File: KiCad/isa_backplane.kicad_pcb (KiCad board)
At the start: 2 copper layers, 116.8 x 154.9 mm, 61 parts, among them P1 POWER, P2 POWER_SW, P3 POWER_LED, SW1 POWER, U1 74HCT74, U2 74HCT14, U3 LM7905CT

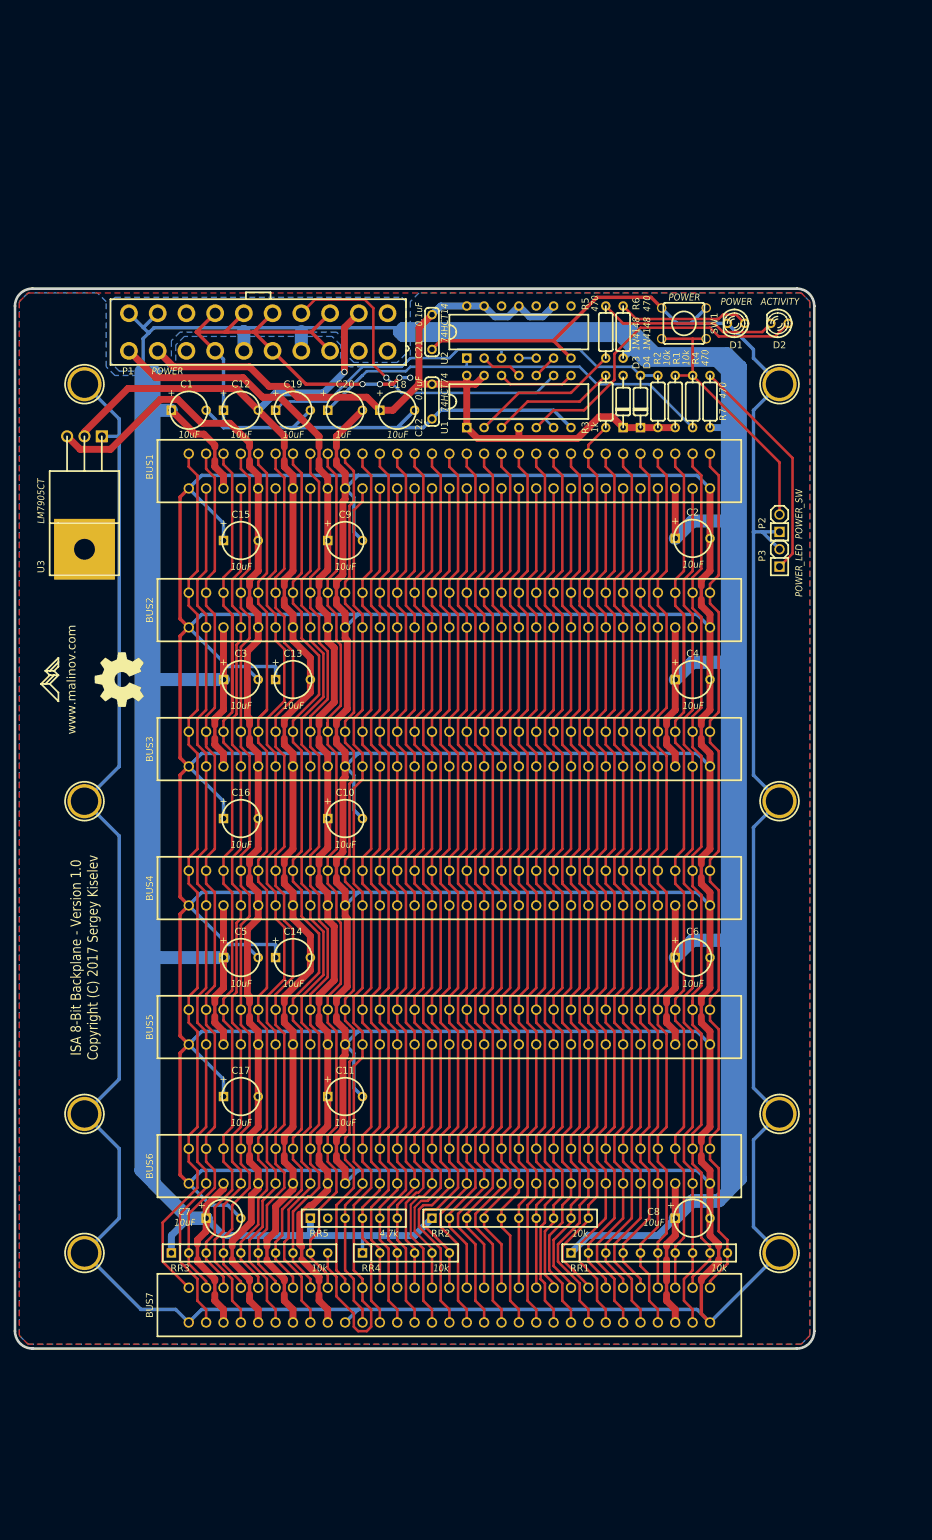
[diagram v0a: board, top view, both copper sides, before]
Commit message: Add two ISA slots
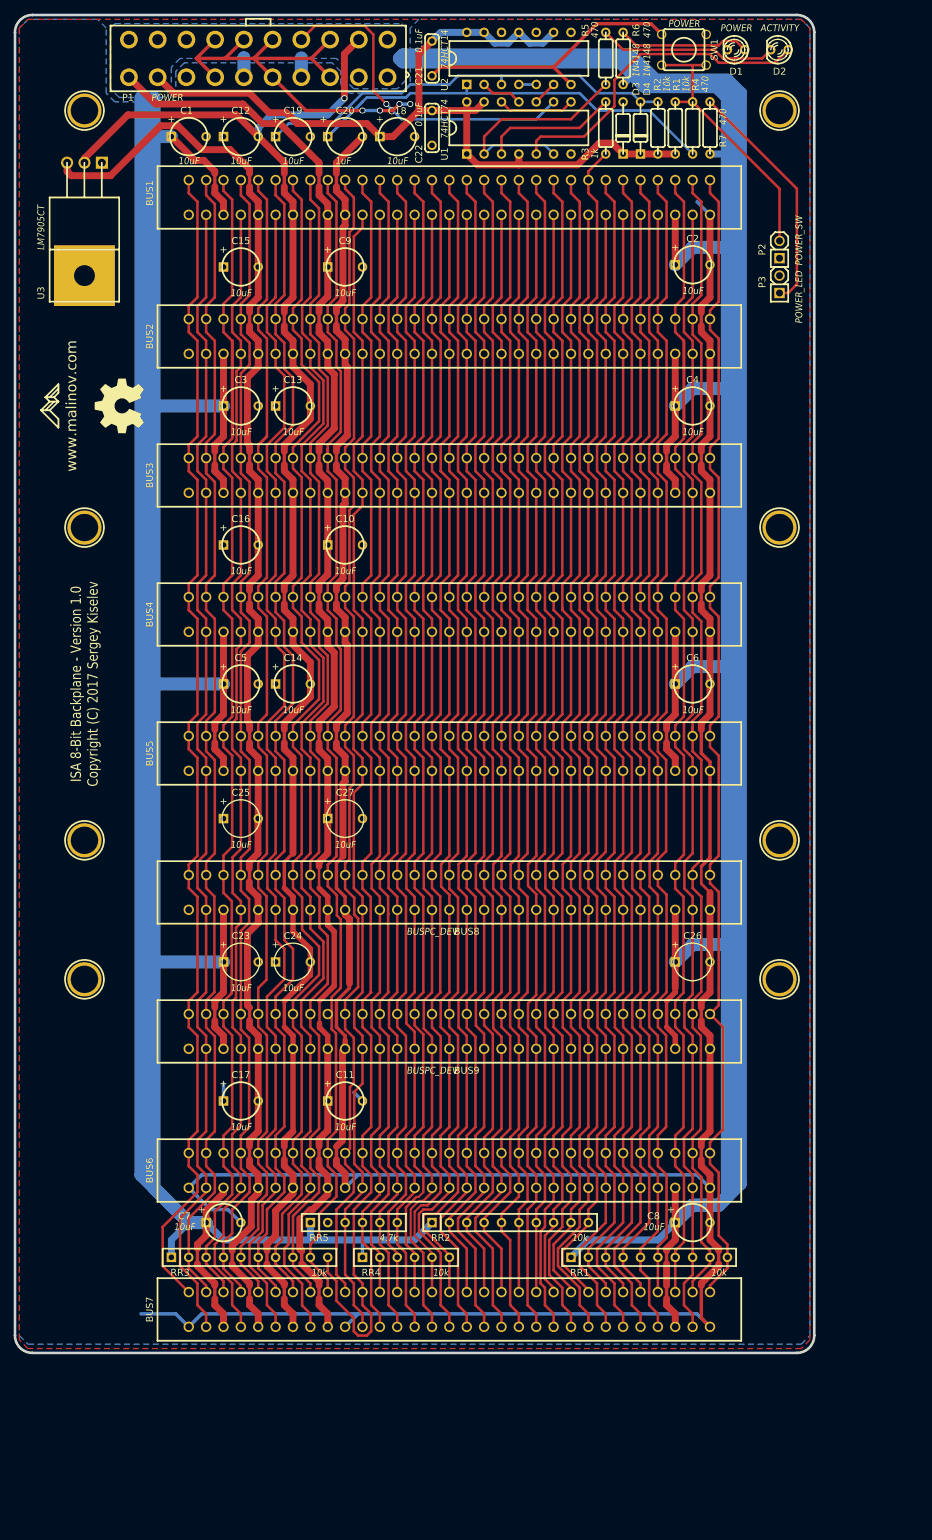
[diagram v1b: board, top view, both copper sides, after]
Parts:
- added BUS8: BUSPC_DEV, My_Components:Conn_Edge_ISA8, F.Cu at (114.3, 139.1)
- added BUS9: BUSPC_DEV, My_Components:Conn_Edge_ISA8, F.Cu at (114.3, 159.4)
- added C23: 10uF, My_Components:Cap_Tant_508, F.Cu at (83.8, 149.2)
- added C24: 10uF, My_Components:Cap_Tant_508, F.Cu at (91.4, 149.2)
- added C25: 10uF, My_Components:Cap_Tant_508, F.Cu at (83.8, 128.3)
- added C26: 10uF, My_Components:Cap_Tant_508, F.Cu at (149.9, 149.2)
- added C27: 10uF, My_Components:Cap_Tant_508, F.Cu at (99.1, 128.3)
- moved C10 40.0 mm to (99.1, 88.3)
- moved C16 40.0 mm to (83.8, 88.3)
- moved BUS2 40.0 mm to (114.3, 57.8)
- moved BUS1 40.0 mm to (114.3, 37.5)
- moved BUS3 40.0 mm to (114.3, 78.1)
- moved BUS4 40.0 mm to (114.3, 98.4)
- moved BUS5 40.0 mm to (114.3, 118.8)
- moved C1 40.0 mm to (76.2, 28.6)
- moved C12 40.0 mm to (83.8, 28.6)
- moved C13 40.0 mm to (91.4, 68.0)
- moved C14 40.0 mm to (91.4, 108.6)
- moved C18 40.0 mm to (106.7, 28.6)
- moved C19 40.0 mm to (91.4, 28.6)
- moved C2 40.0 mm to (149.9, 47.3)
- moved C20 40.0 mm to (99.1, 28.6)
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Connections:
- net /~0WS renamed /~{0WS}
- net /~DACK0 renamed /~{DACK0}
- net /~DACK1 renamed /~{DACK1}
- net /~DACK2 renamed /~{DACK2}
- net /~DACK3 renamed /~{DACK3}
- net /~IOCHK renamed /~{IOCHK}
- net /~IOR renamed /~{IOR}
- net /~IOW renamed /~{IOW}
- net /~MEMR renamed /~{MEMR}
- net /~MEMW renamed /~{MEMW}
- net /~PS_ON renamed /~{PS_ON}
- P1 pad 1: Net-(P1-Pad1) -> unconnected-(P1-3.3V-Pad1)
- P1 pad 11: Net-(P1-Pad11) -> unconnected-(P1-3.3V-Pad11)
- P1 pad 2: Net-(P1-Pad2) -> unconnected-(P1-3.3V-Pad2)
- P1 pad 8: Net-(P1-Pad8) -> unconnected-(P1-PWR_OK-Pad8)
- RR5 pad 2: Net-(RR5-Pad2) -> unconnected-(RR5-Pad2)
- U2 pad 10: Net-(U2-Pad10) -> unconnected-(U2-Pad10)
- U2 pad 12: Net-(U2-Pad12) -> unconnected-(U2-Pad12)
- U2 pad 8: Net-(U2-Pad8) -> unconnected-(U2-Pad8)
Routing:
- net GND: track 1559.7 -> 630.6 mm
- net /+5V: track 951.6 -> 1125.0 mm
- net /-12V: track 204.3 -> 249.9 mm
- net /D2: track 134.5 -> 179.4 mm
- net /-5V: track 171.2 -> 215.5 mm
- net /~{0WS}: track 133.8 -> 177.8 mm
- net /D3: track 132.4 -> 176.2 mm
- net /D1: track 136.4 -> 180.2 mm
- net /DRQ2: track 132.4 -> 176.2 mm
- net /12V: track 173.5 -> 216.9 mm
- net /A0: track 129.3 -> 172.6 mm
- net /IORDY: track 129.3 -> 172.6 mm
- net /A19: track 129.3 -> 172.1 mm
- net /A18: track 129.3 -> 172.0 mm
- net /A16: track 130.9 -> 173.6 mm
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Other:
- board size 116.8 x 154.9 mm -> 116.8 x 195.6 mm
- net class Default removed
- net class Power removed

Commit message: Adjust mounting holes for ATX form factor
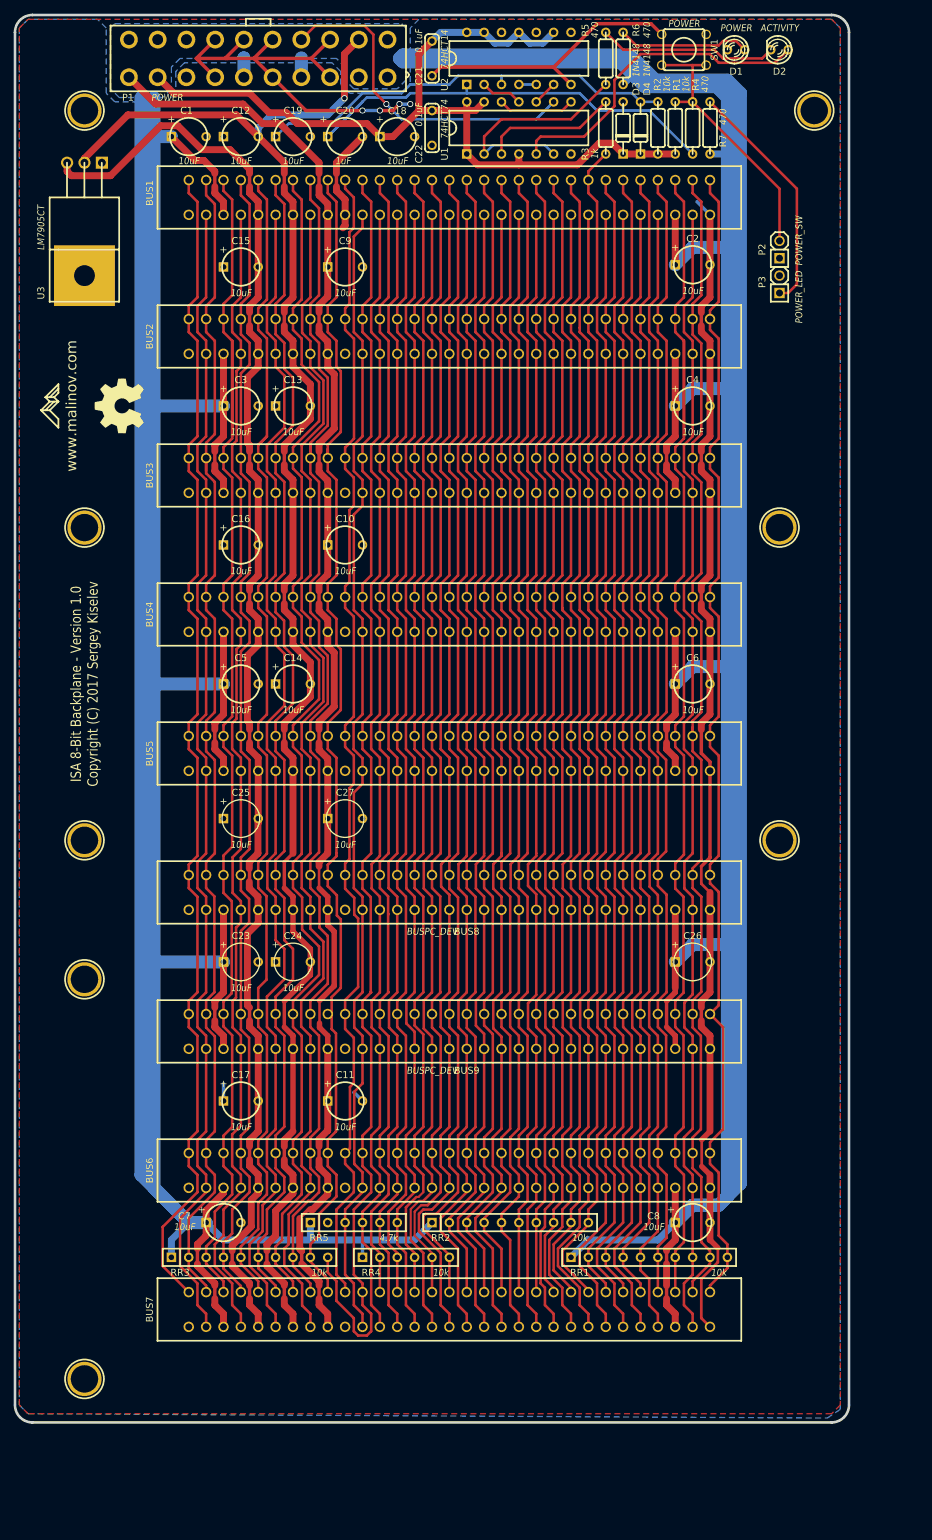
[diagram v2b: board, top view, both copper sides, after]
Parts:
- moved HOLE4 117.2 mm to (61.0, 210.2)
- moved HOLE3 5.08 mm to (167.6, 24.8)
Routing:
- net GND: track 630.6 -> 303.4 mm
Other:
- board size 116.8 x 195.6 mm -> 121.9 x 205.7 mm

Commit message: Move resistor arrays to the bottom
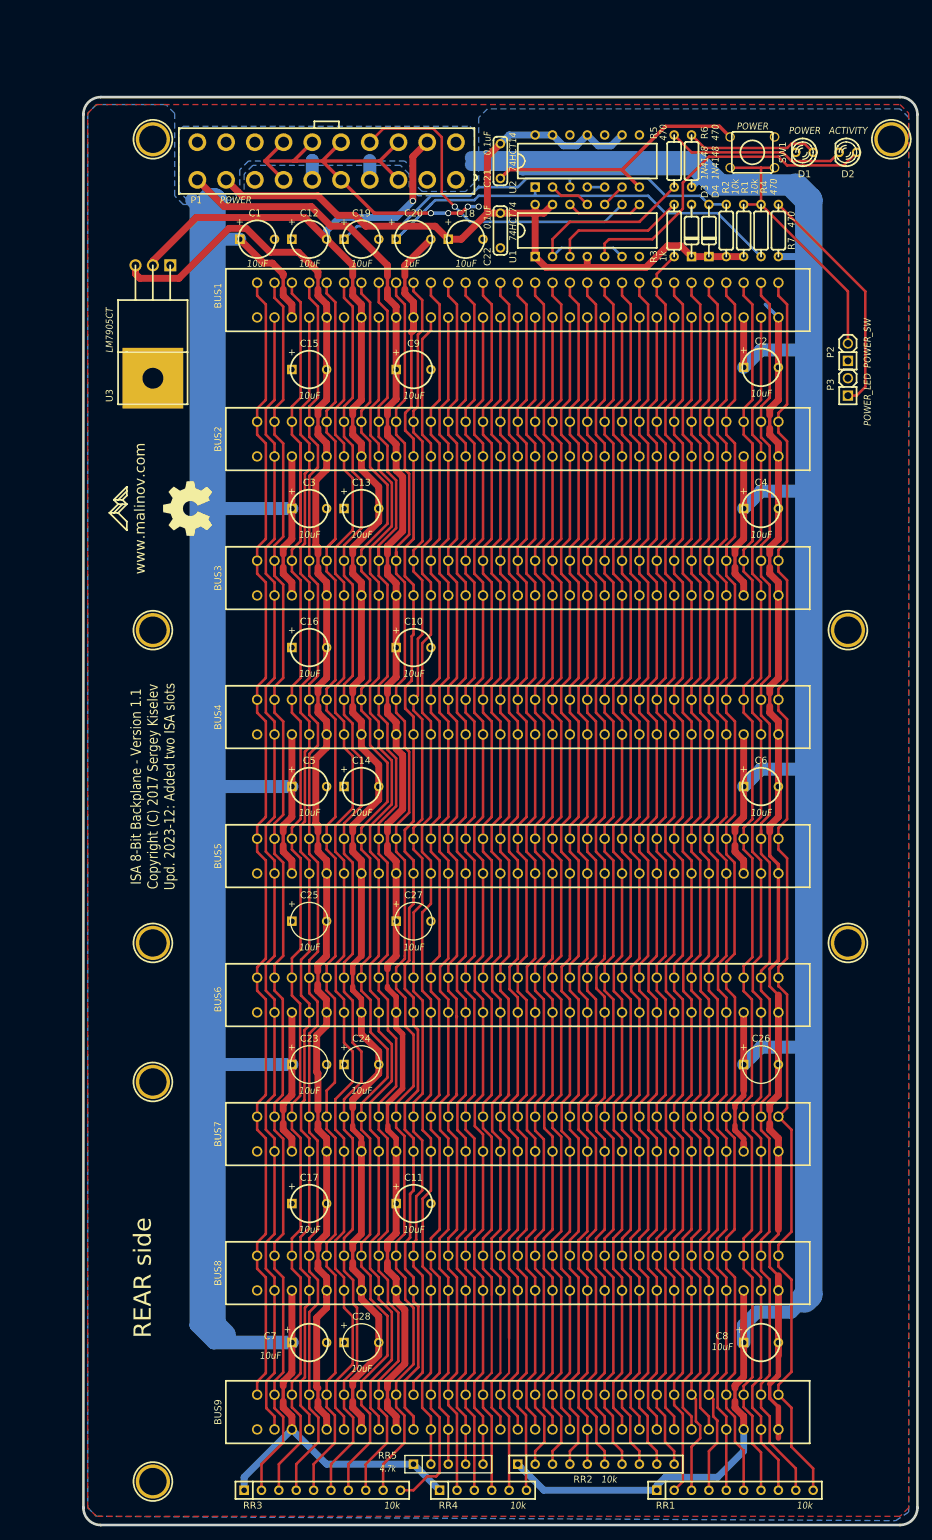
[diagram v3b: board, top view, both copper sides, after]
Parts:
- added C28: 10uF, My_Components:Cap_Tant_508, F.Cu at (101.4, 204.9)
- RR5: footprint my_components:Conn_SIL6 -> My_Components:Conn_SIL5
- moved RR5 37.9 mm to (114.1, 222.6)
- moved RR2 37.5 mm to (135.7, 222.6)
- moved RR1 36.3 mm to (156.1, 226.5)
- moved RR4 35.9 mm to (119.2, 226.5)
- moved RR3 35.7 mm to (95.7, 226.5)
- moved C7 21.6 mm to (93.8, 204.9)
- moved C8 20.2 mm to (159.9, 204.9)
- moved U1 18.0 mm to (134.5, 42.3)
- moved BUS2 18.0 mm to (124.3, 72.8)
- moved U2 18.0 mm to (134.5, 32.1)
- moved BUS1 18.0 mm to (124.3, 52.5)
- moved BUS3 18.0 mm to (124.3, 93.1)
- moved BUS4 18.0 mm to (124.3, 113.4)
- moved BUS5 18.0 mm to (124.3, 133.8)
- moved BUS6 18.0 mm to (124.3, 154.1)
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- renumbered BUS8 to BUS6, BUS9 to BUS7, BUS6 to BUS8, BUS7 to BUS9
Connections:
- RR5 pad 2: unconnected-(RR5-Pad2) -> /~{MEMW}
- RR5 pad 3: /~{MEMW} -> /~{MEMR}
- RR5 pad 4: /~{MEMR} -> /~{IOW}
- RR5 pad 5: /~{IOW} -> /~{IOR}
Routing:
- net GND: track 303.4 -> 469.3 mm
- net /+5V: track 1125.0 -> 973.3 mm
- net /D2: track 179.4 -> 195.2 mm
- net /D0: track 176.7 -> 192.4 mm
- net /A0: track 172.6 -> 188.1 mm
- net /A3: track 172.8 -> 187.8 mm
- net /A2: track 184.8 -> 199.9 mm
- net /A1: track 173.2 -> 188.3 mm
- net /D1: track 180.2 -> 195.0 mm
- net /D3: track 176.2 -> 190.5 mm
- net /D5: track 173.0 -> 186.7 mm
- net /D7: track 174.9 -> 188.6 mm
- net /D6: track 187.0 -> 200.7 mm
- net /D4: track 174.8 -> 188.5 mm
- net /A19: track 172.1 -> 185.5 mm
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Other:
- board size 121.9 x 205.7 mm -> 121.9 x 208.7 mm
- board text added: "ISA 8-Bit Backplane - Version 1.1 Copyright (C) 2017 Sergey Kiselev Upd. 2023-12: Added two ISA slots"
- board text added: "REAR side"
- board text removed: "ISA 8-Bit Backplane - Version 1.0 Copyright (C) 2017 Sergey Kiselev"

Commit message: Version 1.1
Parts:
- added HOLE10: HOLE, My_Components:Hole_4mm, F.Cu at (172.7, 225.2)
- added HOLE9: HOLE, My_Components:Hole_4mm, F.Cu at (172.7, 166.8)
- BUS1, BUS2, BUS3, BUS4, BUS5, BUS8, BUS9: footprint my_components:Conn_Edge_ISA8 -> My_Components:Conn_Edge_ISA8
- C1, C10, C11, C12, C13, C14, C15, C16, C17, C18, C19, C2, C20, C3, C4, C5, C6, C7, C8, C9: footprint my_components:Cap_Tant_508 -> My_Components:Cap_Tant_508
- C21: footprint my_components:Cap_Cer_508 -> My_Components:Cap_Cer_762
- C22: footprint my_components:Cap_Cer_508 -> My_Components:Cap_Cer_508
- D1, D2: footprint my_components:LED_3mm -> My_Components:LED_3mm
- D3, D4: footprint my_components:Diode_762 -> My_Components:Diode_762
- HOLE1, HOLE2, HOLE3, HOLE4, HOLE5, HOLE6, HOLE7, HOLE8: footprint my_components:Hole_4mm -> My_Components:Hole_4mm
- P1: footprint my_components:Conn_Power_ATX_20pin -> My_Components:Conn_Power_ATX_20pin
- P2, P3: footprint my_components:Conn_Pin_Header_2x1_2.54mm -> My_Components:Conn_Pin_Header_2x1_2.54mm
- R1, R2, R3, R4, R5, R6, R7: footprint my_components:Res_762 -> My_Components:Res_762
- RR1, RR2, RR3: footprint my_components:Conn_SIL10 -> My_Components:Conn_SIL10
- RR4: footprint my_components:Conn_SIL6 -> My_Components:Conn_SIL6
- SW1: footprint my_components:Switch_Tactile_6mm -> My_Components:Switch_Tactile_6mm
- U1, U2: footprint my_components:IC_DIP14_300 -> My_Components:IC_DIP14_300
- U3: footprint my_components:IC_TO220-3_Horiz -> My_Components:IC_TO220-3_Vert
- moved R7 12.7 mm to (172.5, 50.0), turned to 90 degrees
- moved D2 7.81 mm to (171.4, 38.6), turned to 0 degrees
- moved D1 5.26 mm to (171.4, 30.5), turned to 0 degrees
- moved C21 2.61 mm to (124.2, 31.1), turned to 90 degrees
- moved D3 2.54 mm to (152.2, 42.3)
- moved R1 2.54 mm to (159.9, 42.3)
- moved R6 2.54 mm to (152.2, 32.1)
- moved RR1 2.54 mm to (153.5, 226.5)
- moved C12 2.54 mm to (96.4, 43.6)
- moved C19 2.54 mm to (104.0, 43.6)
- moved P1 2.54 mm to (98.9, 32.1)
- moved C1 2.54 mm to (88.7, 43.6)
- moved C18 2.54 mm to (119.2, 43.6)
- moved C20 2.54 mm to (111.6, 43.6)
- moved C22 2.54 mm to (124.3, 42.3)
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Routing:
- net GND: track 469.3 -> 640.3 mm, vias 4 -> 2
- net /+5V: track 973.3 -> 1030.7 mm
- net Net-(P3-P1): track 35.0 -> 15.5 mm
- net Net-(D2-K): track 26.2 -> 29.5 mm
- net /D0: track 192.4 -> 189.8 mm
- net /A1: track 188.3 -> 185.9 mm
- net /-12V: track 250.6 -> 252.8 mm
- net /A7: track 187.0 -> 189.0 mm
- net /A0: track 188.1 -> 186.3 mm
- net /A6: track 186.0 -> 187.7 mm
- net /A4: track 186.0 -> 187.1 mm
- net /OSC: track 180.8 -> 179.8 mm
- net /ALE: track 179.8 -> 180.9 mm
- net /A5: track 186.0 -> 187.0 mm
- net /~{PS_ON}: track 49.3 -> 50.3 mm
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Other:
- rule pad_to_mask_clearance: 0.254 -> 0
